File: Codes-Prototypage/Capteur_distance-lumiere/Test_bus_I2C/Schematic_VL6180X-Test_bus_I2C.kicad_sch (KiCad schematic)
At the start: 4 parts

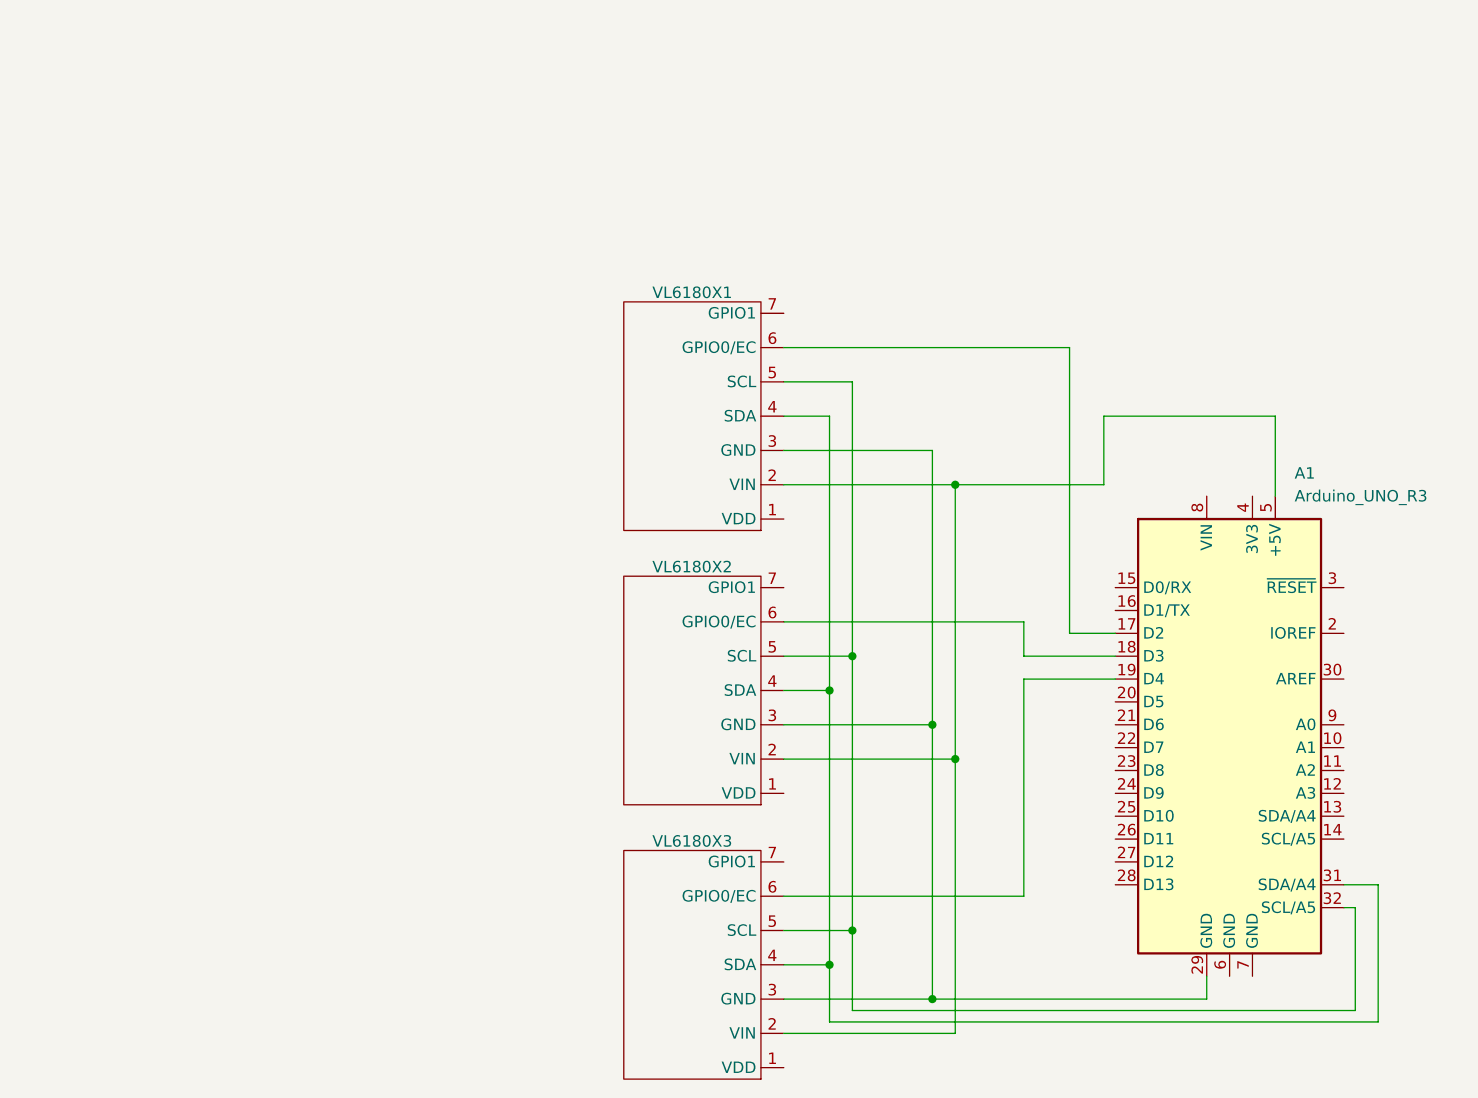
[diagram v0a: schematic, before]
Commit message: feat: Configuration de taille de page et création du PDF pour la schematic
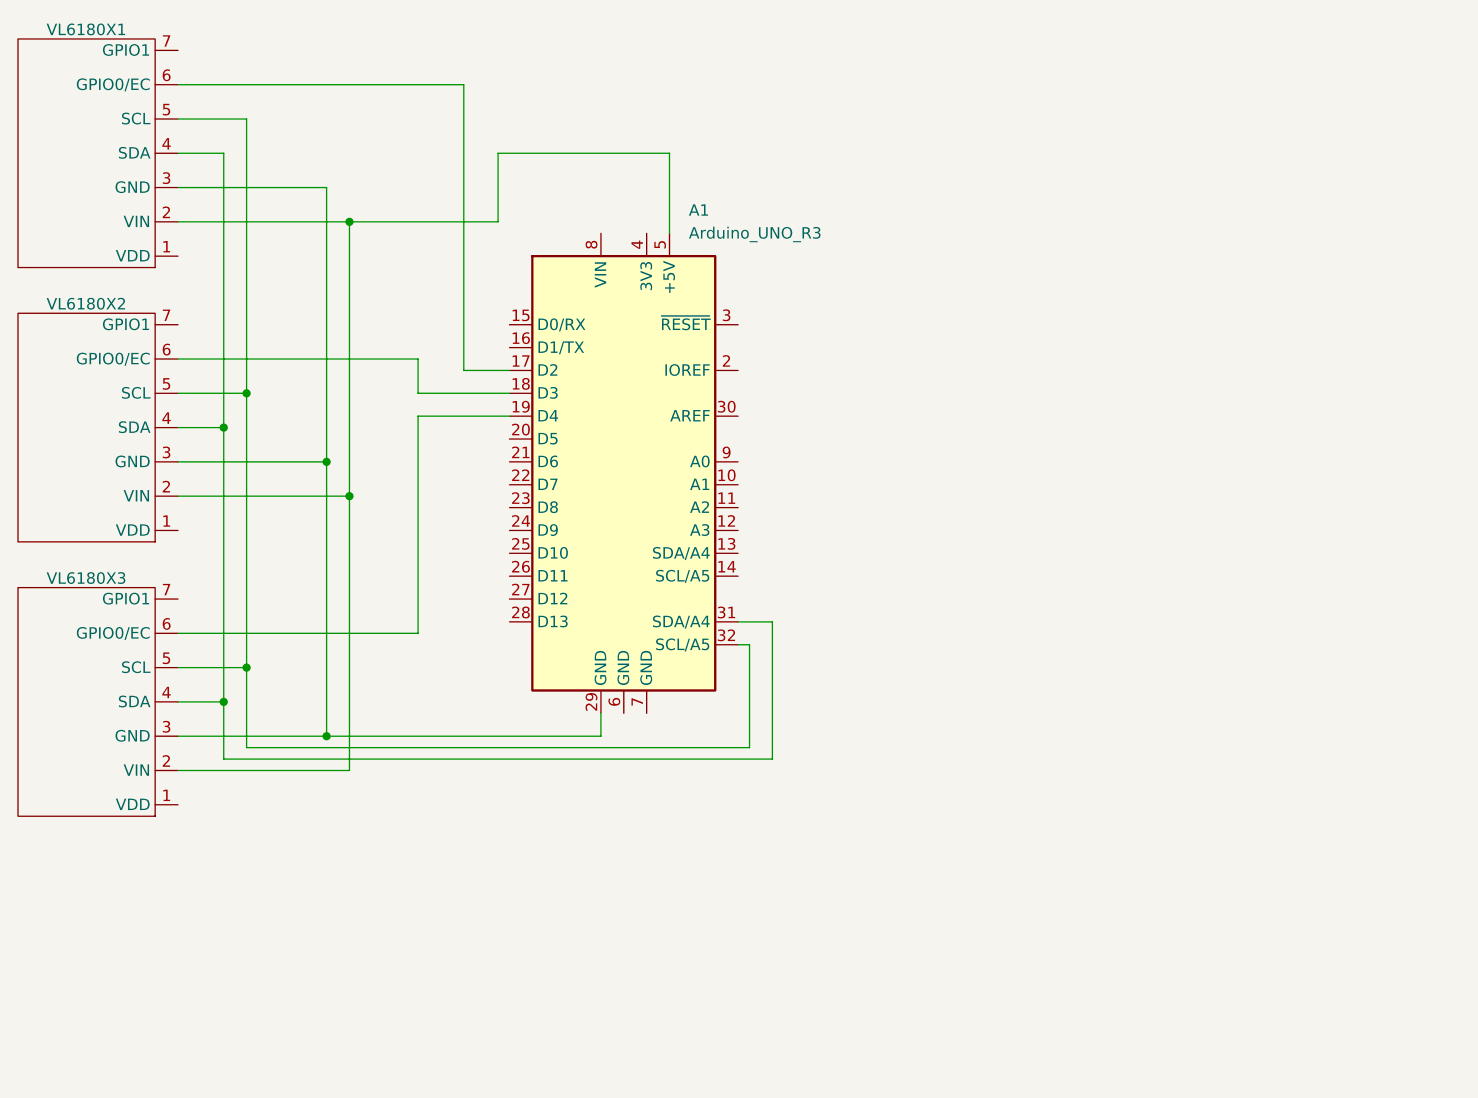
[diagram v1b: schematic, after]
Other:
- title: (none) -> Schematic VL6180X - Test bus I2C
- moved on the sheet: A1, VL6180X1, VL6180X2, VL6180X3
